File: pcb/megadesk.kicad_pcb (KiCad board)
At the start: 2 copper layers, 41.7 x 32.2 mm, 28 parts, among them J2 FFC, J3 AVR-ISP-6, J4 Interface, U1 7812, U2 HT7550-1, U3 ATtiny841-SS, U4 MCP2003B

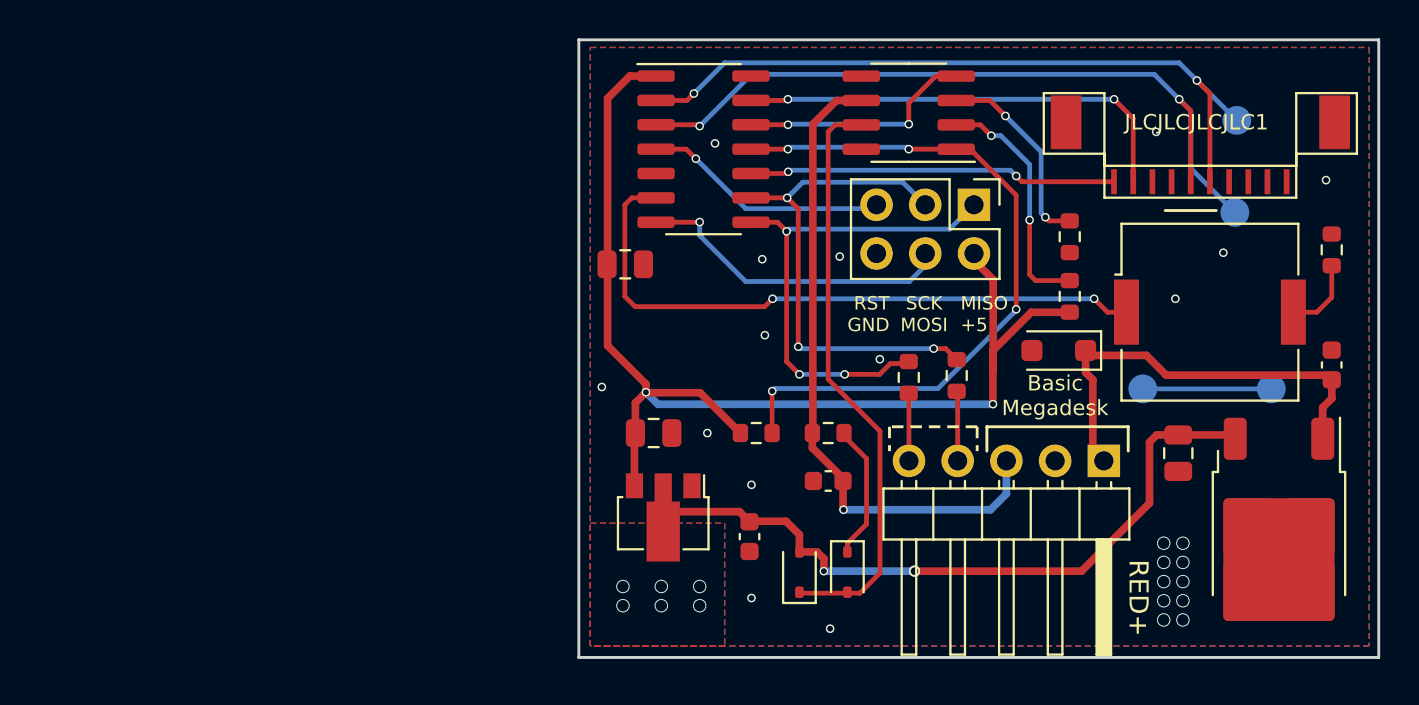
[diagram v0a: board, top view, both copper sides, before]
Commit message: Add some component, change resistor value and change board size
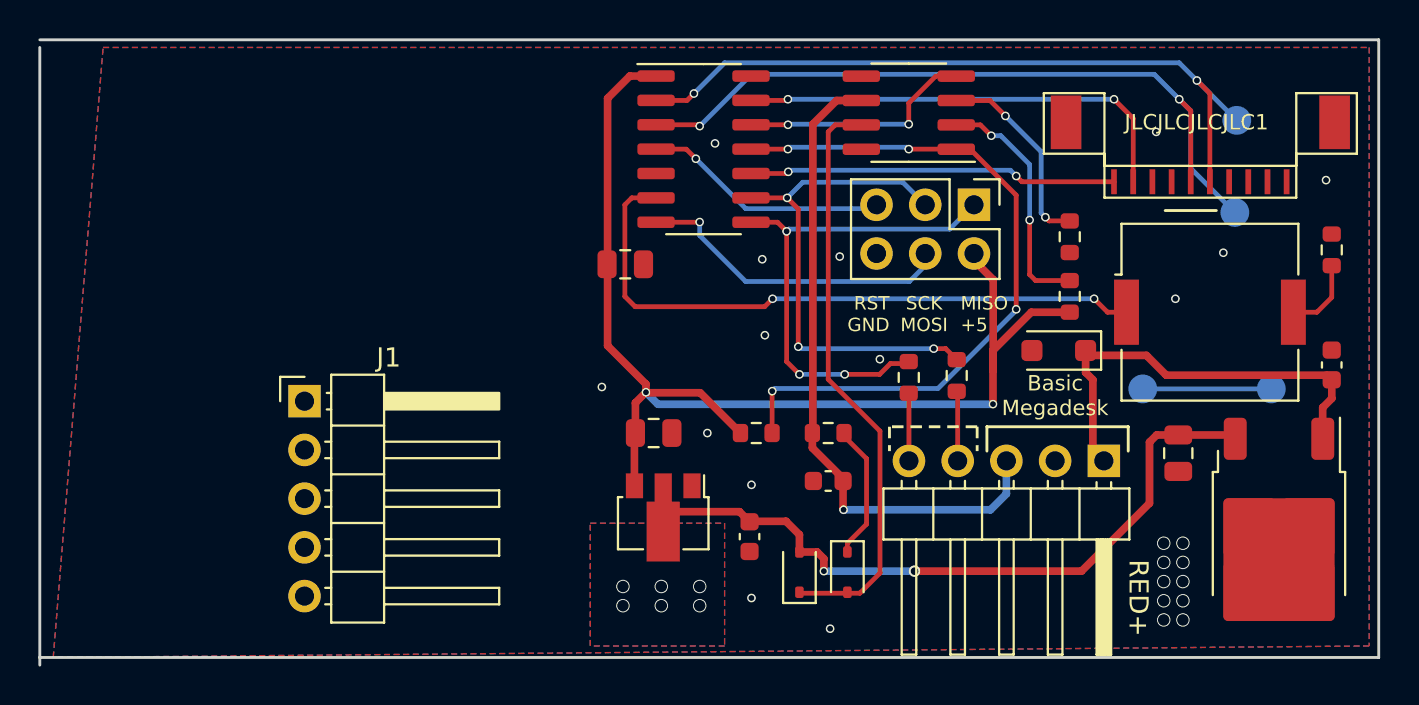
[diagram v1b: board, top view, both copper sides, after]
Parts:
- added J1: Interface, Connector_PinHeader_2.54mm:PinHeader_1x05_P2.54mm_Horizontal, F.Cu at (84.9, 123.4)
- R1: value 1k -> 2k
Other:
- board size 41.7 x 32.2 mm -> 69.8 x 32.6 mm
